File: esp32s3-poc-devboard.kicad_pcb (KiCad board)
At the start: 4 copper layers, 74 x 66.8 mm, 108 parts, among them J1 24VDC, J2 Conn_01x01_Pin, J3 USB_C_Receptacle_USB2.0_14P, J4 USB_C_Receptacle_USB2.0_14P, J5 Screw_Terminal_01x06, J6 Conn_Coaxial, J7 Conn_01x16_Pin, J8 Screw_Terminal_01x04, Q3 MMDT5551, SW1 SW_Push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

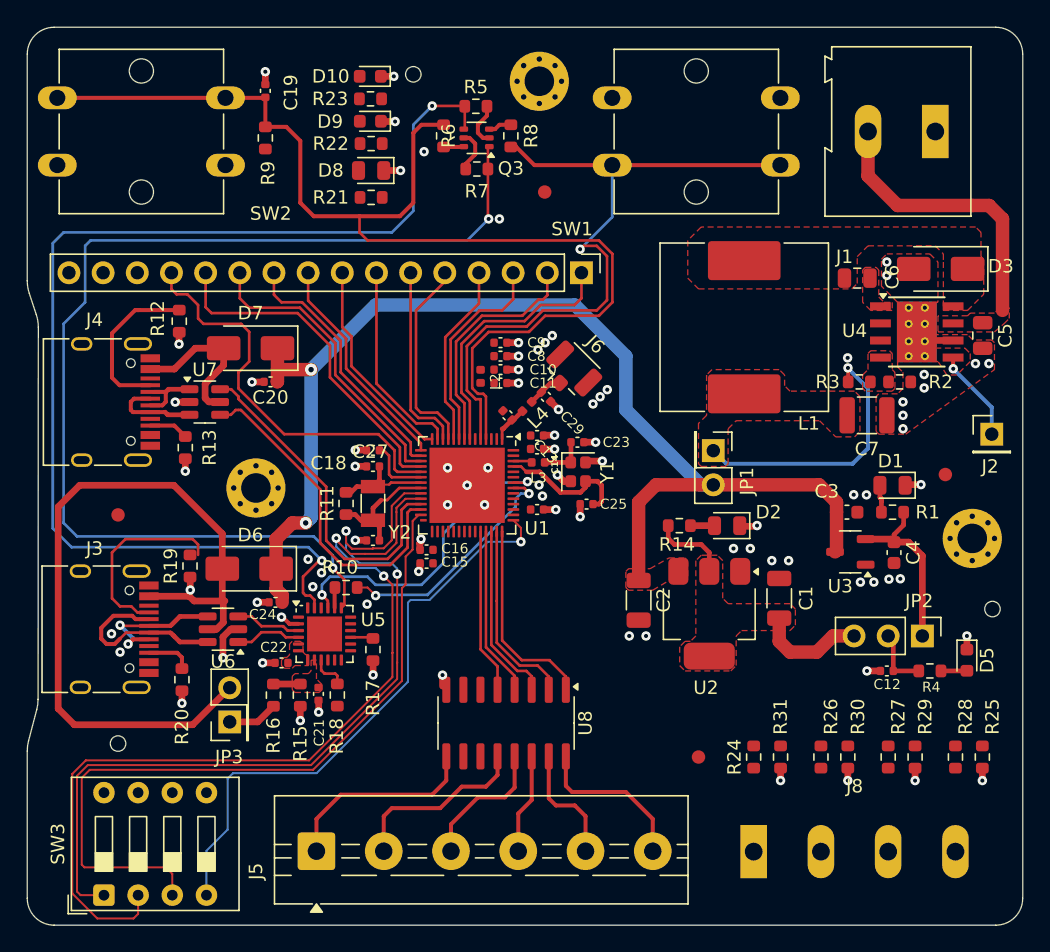
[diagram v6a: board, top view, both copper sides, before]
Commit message: add 24v I routing
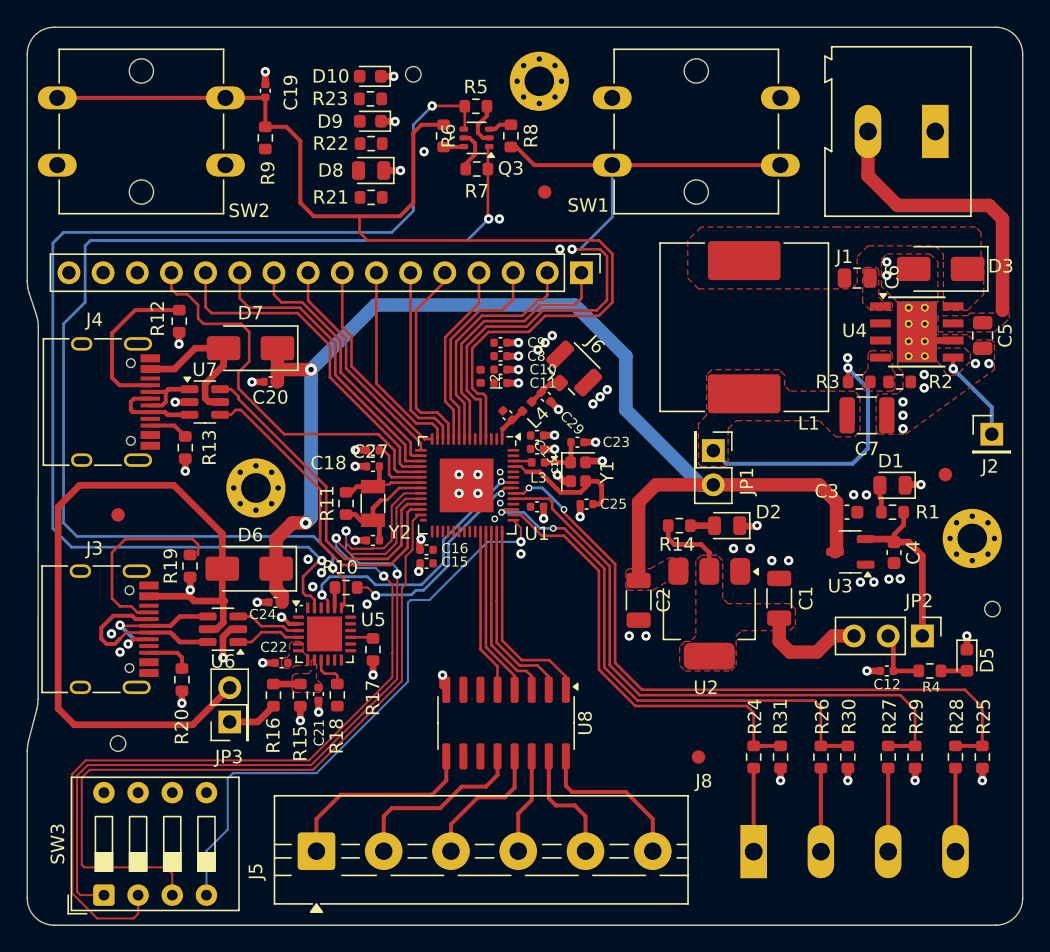
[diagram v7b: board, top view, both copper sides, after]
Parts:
- moved C17 0.20 mm to (160.4, 86.4)
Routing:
- net Net-(U1-MTMS/JTAG/GPIO42): track 0.00 -> 50.8 mm, vias 0 -> 2
- net Net-(U1-MTDI/JTAG/GPIO41): track 0.00 -> 45.6 mm
- net Net-(U1-MTDO/JTAG/GPIO40): track 0.00 -> 39.9 mm, vias 0 -> 2
- net Net-(U1-MTCK/JTAG/GPIO39): track 0.00 -> 32.7 mm
- net Net-(J8-Pin_4): track 0.00 -> 6.21 mm
- net Net-(J8-Pin_3): track 0.00 -> 6.21 mm
- net Net-(J8-Pin_2): track 0.00 -> 6.21 mm
- net Net-(J8-Pin_1): track 0.00 -> 6.21 mm
- net U0RXD: track 23.6 -> 20.9 mm
- net Net-(U1-U0TXD/PROG/GPIO43): track 18.3 -> 16.3 mm
- net BOOT: track 52.9 -> 53.9 mm
- net GND: vias 86 -> 88

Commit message: add status leds routing
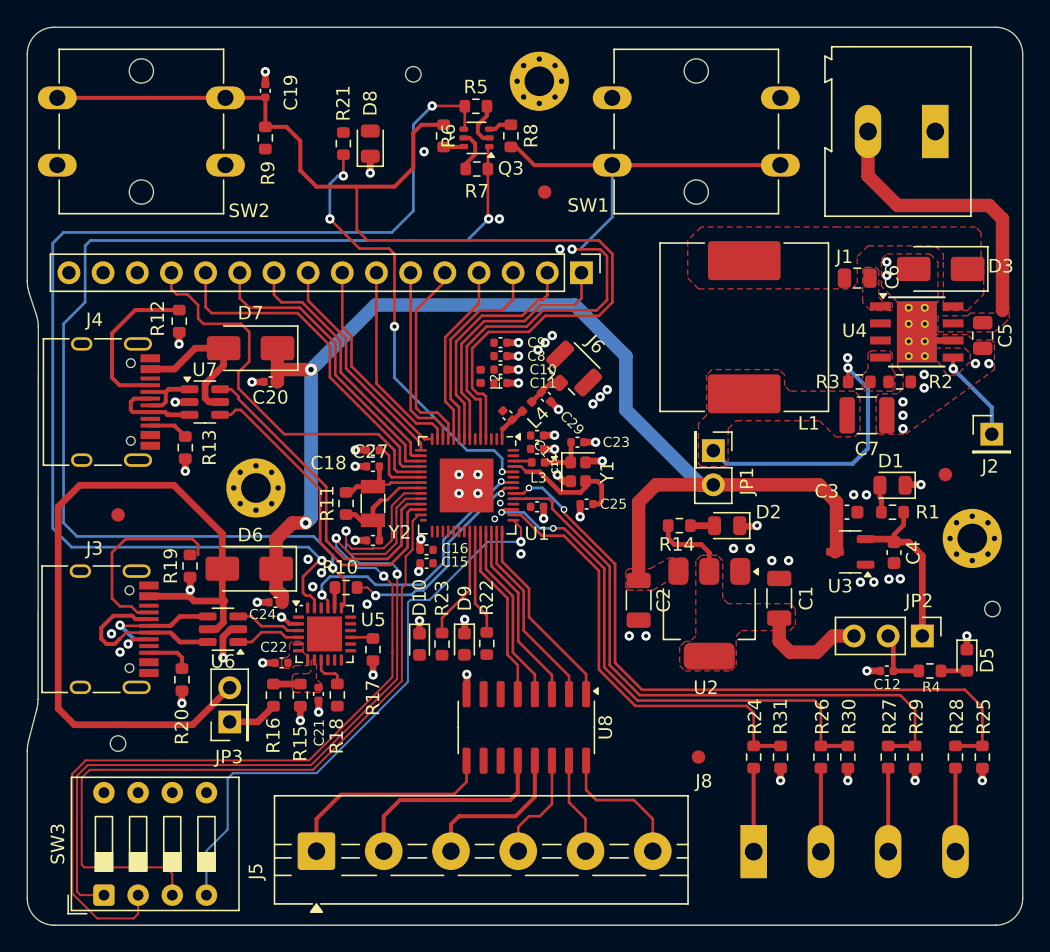
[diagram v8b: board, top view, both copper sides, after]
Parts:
- moved D10 42.4 mm to (151.7, 96.6), turned to -90 degrees
- moved R23 40.9 mm to (153.3, 96.6), turned to -90 degrees
- moved D9 39.5 mm to (155.0, 96.6), turned to -90 degrees
- moved R22 38.1 mm to (156.7, 96.6), turned to -90 degrees
- moved R21 4.50 mm to (146.0, 59.4), turned to 90 degrees
- moved D8 2.00 mm to (148.0, 59.4), turned to 90 degrees
- moved U8 1.54 mm to (159.6, 102.8)
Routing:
- net Net-(U1-GPIO46): track 0.00 -> 33.2 mm, vias 0 -> 4
- net Net-(U1-SPICLK_N/GPIO48): track 0.00 -> 8.40 mm
- net Net-(U1-SPICLK_P/GPIO47): track 0.00 -> 7.85 mm
- net CHIP_PU: track 85.7 -> 83.3 mm
- net Net-(J5-Pin_2): track 13.7 -> 15.7 mm
- net Net-(J5-Pin_5): track 9.00 -> 7.23 mm
- net Net-(J5-Pin_6): track 12.1 -> 10.4 mm
- net Net-(J5-Pin_3): track 10.2 -> 11.8 mm
- net Net-(J5-Pin_1): track 15.0 -> 16.3 mm
- net Net-(U1-GPIO34): track 12.6 -> 13.6 mm
- net Net-(U1-GPIO33): track 12.3 -> 13.2 mm
- net Net-(J5-Pin_4): track 7.46 -> 8.23 mm
- net Net-(U1-GPIO35): track 13.4 -> 14.0 mm
- net GND: vias 88 -> 87
